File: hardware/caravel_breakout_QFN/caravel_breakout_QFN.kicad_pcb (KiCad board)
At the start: 2 copper layers, 25.4 x 25.4 mm, 20 parts, among them J1 Conn_01x14_Female, J2 Conn_01x14_Female, J3 Conn_01x14_Female, J4 Conn_01x14_Female, T1 Logo, T2 Logo, U1 Caravel

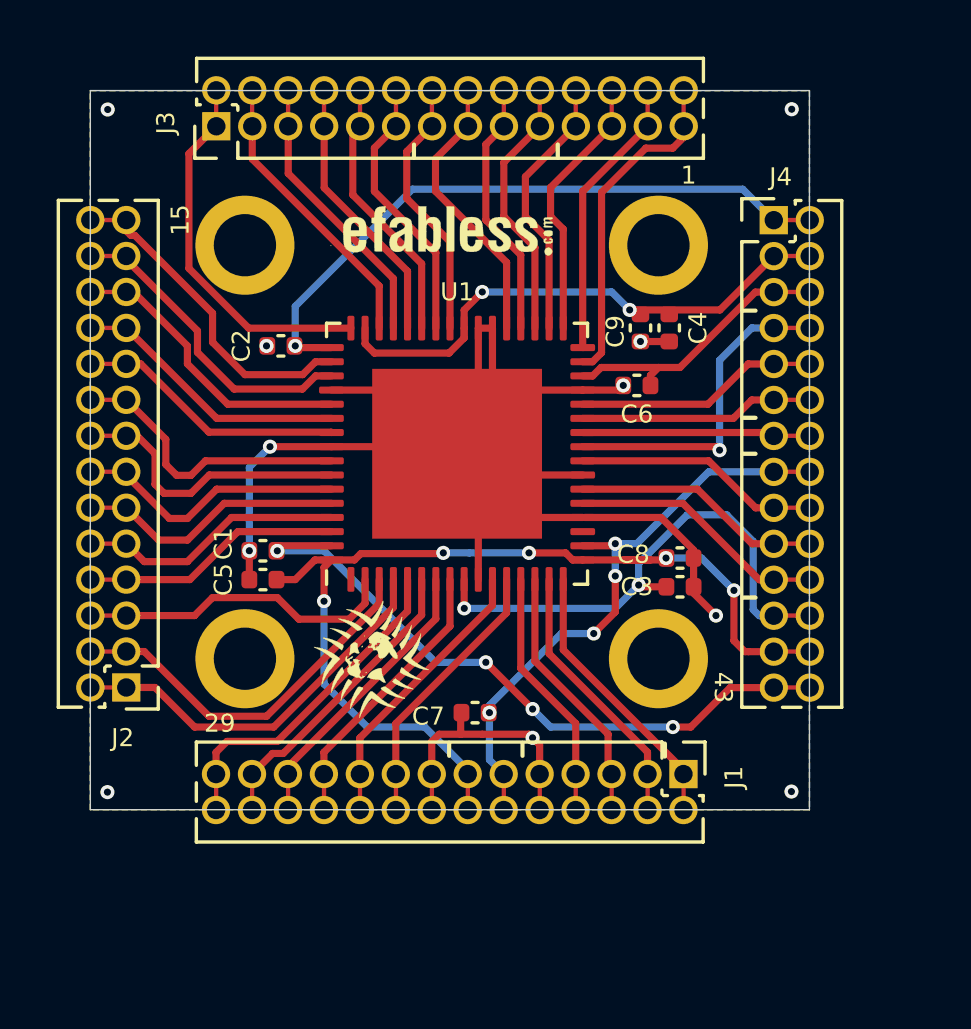
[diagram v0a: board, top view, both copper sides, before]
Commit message: Updated the caravel QFN breakout board connectors
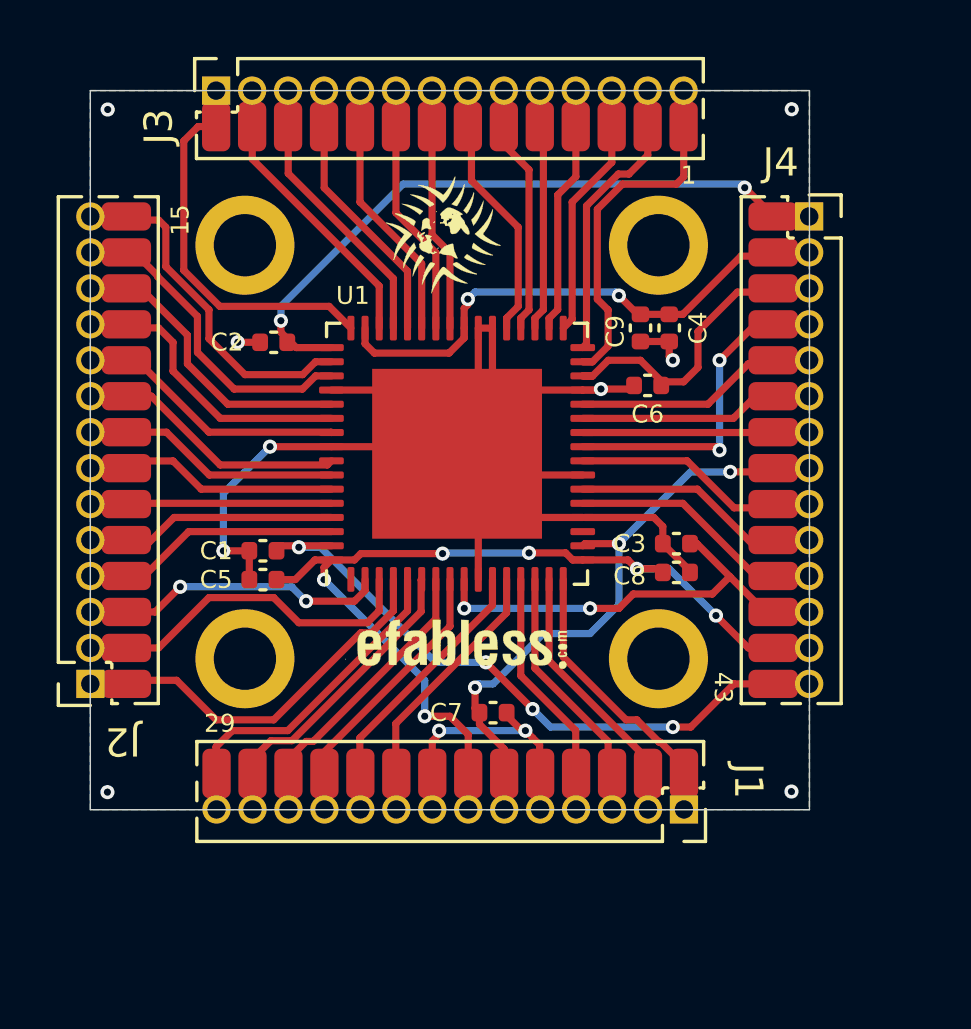
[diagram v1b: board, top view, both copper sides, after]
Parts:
- J1, J2, J3, J4: footprint Connector_PinHeader_1.27mm:PinHeader_2x14_P1.27mm_Vertical -> Caravel_Board:Caravel_Breakout_Connectors_2x14
- T2: footprint Caravel:ef_logo -> Caravel_Board:ef_logo
- moved T1 15.2 mm to (132.8, 81.3)
- moved T2 14.6 mm to (133.5, 95.8)
- moved C3 1.53 mm to (141.1, 92.2), turned to 0 degrees
- moved J4 1.42 mm to (145.2, 79.5)
- moved J1 1.31 mm to (142.5, 101.0)
- moved J3 1.31 mm to (123.7, 76.8)
- moved J2 1.20 mm to (121.0, 98.3)
- moved C7 0.63 mm to (134.6, 98.2), turned to 180 degrees
- moved C8 0.52 mm to (141.1, 93.2)
- moved C6 0.38 mm to (140.1, 86.6)
- moved C2 0.28 mm to (126.9, 85.1)
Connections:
- J1 pad 10: GND -> mprj_io[32]
- J1 pad 11: vccd -> mprj_io[31]
- J1 pad 12: vccd -> mprj_io[30]
- J1 pad 13: vddio -> mprj_io[29]
- J1 pad 14: vddio -> mprj_io[28]
- J1 pad 2: mprj_io[37] -> mprj_io[36]
- J1 pad 3: mprj_io[36] -> mprj_io[35]
- J1 pad 4: mprj_io[36] -> mprj_io[34]
- J1 pad 5: mprj_io[35] -> GND
- J1 pad 6: mprj_io[35] -> vccd
- J1 pad 7: mprj_io[34] -> vddio
- J1 pad 8: mprj_io[34] -> GND
- J1 pad 9: GND -> mprj_io[33]
- J2 pad 10: mprj_io[23] -> mprj_io[18]
- J2 pad 11: mprj_io[22] -> mprj_io[17]
- J2 pad 12: mprj_io[22] -> mprj_io[16]
- J2 pad 13: mprj_io[21] -> mprj_io[15]
- J2 pad 14: mprj_io[21] -> mprj_io[14]
- J2 pad 2: mprj_io[27] -> mprj_io[26]
- J2 pad 3: mprj_io[26] -> mprj_io[25]
- J2 pad 4: mprj_io[26] -> mprj_io[24]
- J2 pad 5: mprj_io[25] -> mprj_io[23]
- J2 pad 6: mprj_io[25] -> mprj_io[22]
- J2 pad 7: mprj_io[24] -> mprj_io[21]
- J2 pad 8: mprj_io[24] -> mprj_io[20]
- J2 pad 9: mprj_io[23] -> mprj_io[19]
- J3 pad 10: mprj_io[9] -> mprj_io[4]_SCK
- J3 pad 11: mprj_io[8] -> mprj_io[3]_CSB
- J3 pad 12: mprj_io[8] -> mprj_io[2]_SDI
- J3 pad 13: mprj_io[7] -> mprj_io[1]_SDO
- J3 pad 14: mprj_io[7] -> mprj_io[0]
- J3 pad 2: mprj_io[13] -> mprj_io[12]
- J3 pad 3: mprj_io[12] -> mprj_io[11]
- J3 pad 4: mprj_io[12] -> mprj_io[10]
- J3 pad 5: mprj_io[11] -> mprj_io[9]
- J3 pad 6: mprj_io[11] -> mprj_io[8]
- J3 pad 7: mprj_io[10] -> mprj_io[7]
- J3 pad 8: mprj_io[10] -> mprj_io[6]_ser_tx
- J3 pad 9: mprj_io[9] -> mprj_io[5]_ser_rx
- J4 pad 10: gpio -> xclk
- J4 pad 11: Caravel_D1 -> ~{RST}
- J4 pad 12: Caravel_D1 -> vdda2
- J4 pad 13: Caravel_D0 -> vddio
- J4 pad 14: Caravel_D0 -> vccd2
- J4 pad 2: vccd1 -> vdda1
- J4 pad 3: vdda1 -> vdda
- J4 pad 4: vdda1 -> Caravel_SCK
- J4 pad 5: vdda -> gpio
- J4 pad 6: vdda -> Caravel_D1
- J4 pad 7: Caravel_SCK -> Caravel_D0
- J4 pad 8: Caravel_SCK -> vccd
- J4 pad 9: gpio -> Caravel_CSB
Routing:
- net GND: track 68.7 -> 63.4 mm
- net vddio: track 34.7 -> 30.4 mm, vias 5 -> 6
- net vdda2: track 18.7 -> 15.3 mm
- net mprj_io[20]: track 10.1 -> 7.93 mm
- net mprj_io[26]: track 13.5 -> 11.3 mm
- net mprj_io[22]: track 9.32 -> 7.31 mm
- net mprj_io[8]: track 9.55 -> 7.71 mm
- net mprj_io[19]: track 10.2 -> 8.32 mm
- net vccd2: track 23.7 -> 21.9 mm
- net mprj_io[7]: track 9.20 -> 7.39 mm
- net mprj_io[3]_CSB: track 9.28 -> 7.52 mm
- net mprj_io[21]: track 9.50 -> 7.82 mm
- net mprj_io[6]_ser_tx: track 9.71 -> 8.03 mm
- net mprj_io[23]: track 9.22 -> 7.63 mm
- net mprj_io[25]: track 11.2 -> 9.56 mm, vias 0 -> 2
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
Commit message: add gerber files
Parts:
- U1: footprint Package_DFN_QFN:QFN-64-1EP_9x9mm_P0.5mm_EP6x6mm -> Package_DFN_QFN:QFN-64-1EP_9x9mm_P0.5mm_EP7.65x7.65mm
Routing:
- net vdda1: track 17.7 -> 19.4 mm, vias 2 -> 3
- net vddio: track 30.4 -> 31.6 mm, vias 6 -> 4
- net vccd2: track 21.9 -> 22.9 mm

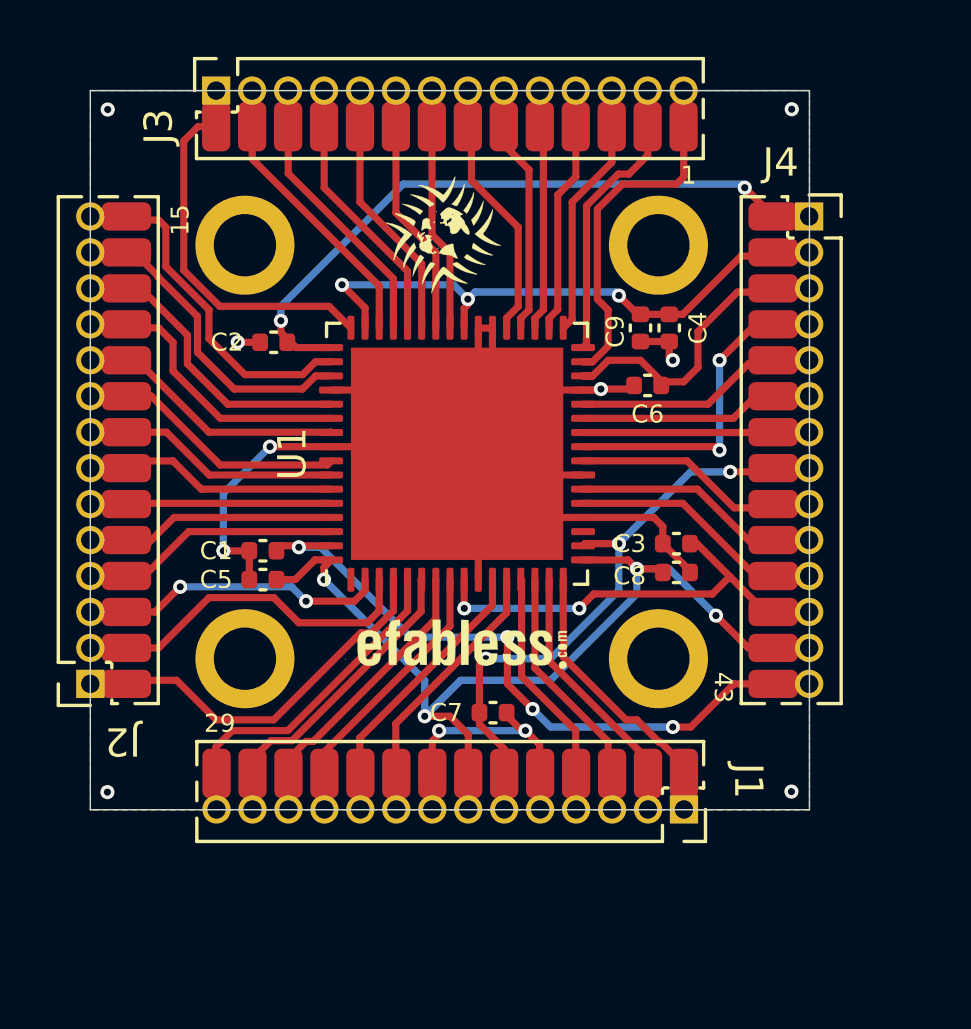
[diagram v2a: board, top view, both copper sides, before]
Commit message: add pads on both sides of caravel breakout board (Rev C)
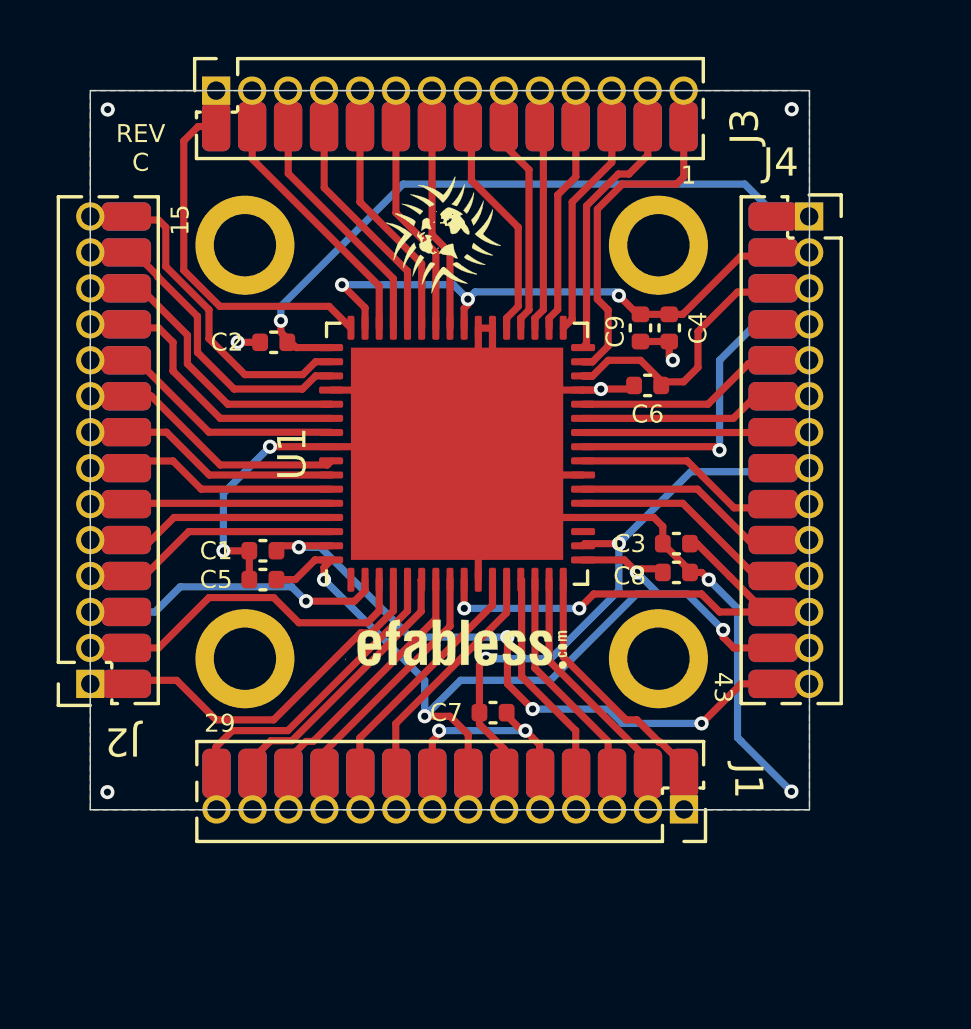
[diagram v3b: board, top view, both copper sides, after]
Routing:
- net GND: track 63.4 -> 72.9 mm, vias 11 -> 12
- net vdda2: track 15.3 -> 16.1 mm
- net vccd1: track 22.5 -> 22.7 mm, vias 2 -> 1
- net vccd: vias 3 -> 2
- net mprj_io[25]: vias 2 -> 1
- net Caravel_SCK: vias 2 -> 1
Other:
- board text added: "C"
- board text added: "REV"

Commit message: update QFN caravel breakout board silkscreen
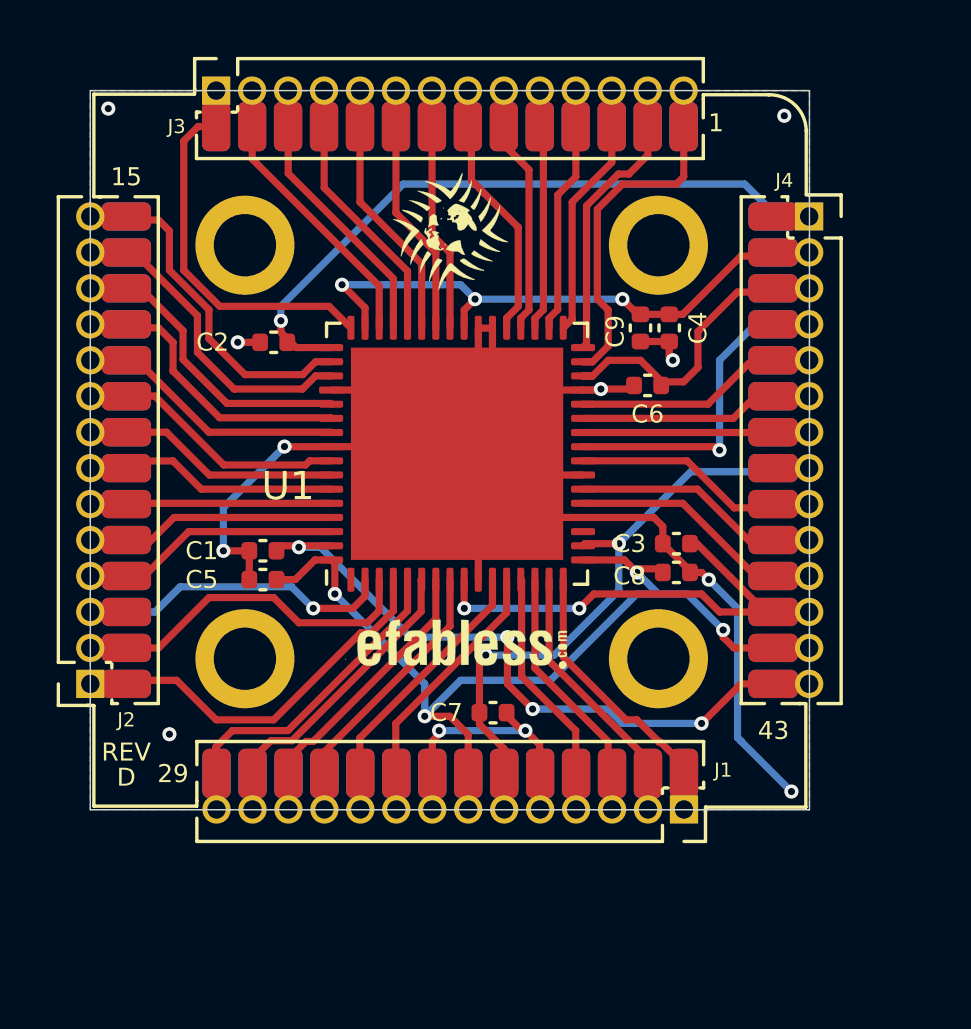
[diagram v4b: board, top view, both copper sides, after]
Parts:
- added ?: , clipboard:dd7ec026-37c5-4c16-b24b-a4168c525ae3, F.Cu at (145.3, 76.7)
- moved T1 0.28 mm to (133.1, 81.2)
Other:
- board text added: "D"
- board text removed: "C"

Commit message: update caravel QFN breakout board with WCSP pinout (V2)
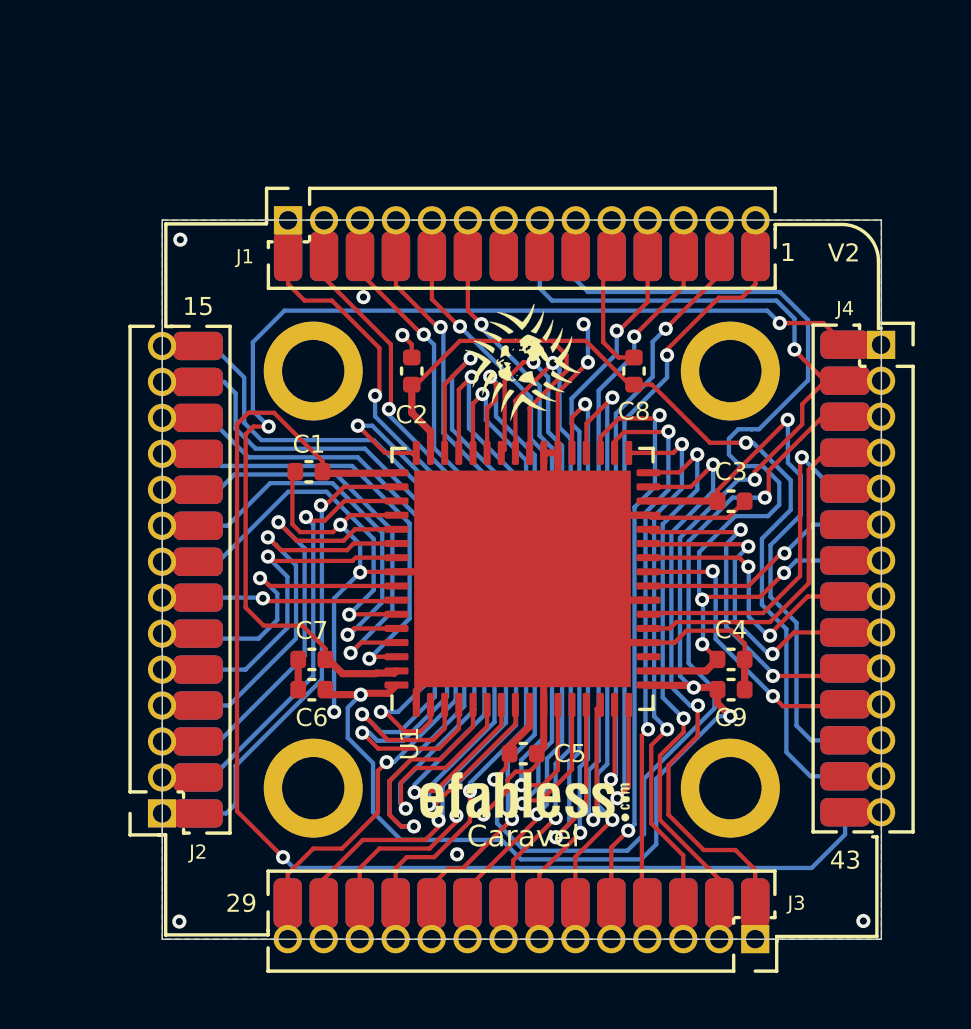
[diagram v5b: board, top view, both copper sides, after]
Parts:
- removed ?: , clipboard:dd7ec026-37c5-4c16-b24b-a4168c525ae3
- T2: footprint Caravel_Board:ef_logo -> Caravel:ef_logo
- moved J3 35.8 mm to (145.0, 105.5), turned to -90 degrees
- moved J1 25.4 mm to (126.2, 81.4), turned to 90 degrees
- moved C6 16.0 mm to (128.2, 97.4), turned to 0 degrees
- moved C9 13.2 mm to (143.0, 97.4), turned to 180 degrees
- moved C4 11.9 mm to (143.0, 96.3), turned to 180 degrees
- moved C5 11.1 mm to (135.7, 99.6), turned to 180 degrees
- moved C8 7.27 mm to (139.6, 86.1), turned to 90 degrees
- moved C7 6.67 mm to (128.2, 96.3), turned to 0 degrees
- moved T2 5.82 mm to (135.7, 101.1)
- moved T1 5.27 mm to (135.6, 85.8)
- moved H2 5.23 mm to (143.0, 100.8)
- moved J2 5.23 mm to (123.6, 102.9)
- moved J4 5.20 mm to (147.7, 84.0)
- moved H1 5.17 mm to (128.3, 100.8)
- moved H3 5.12 mm to (143.0, 86.1)
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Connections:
- C1 pad 2: vccd2 -> vccd1
- C2 pad 1: GND -> vdda1
- C2 pad 2: vccd1 -> GND
- C3 pad 1: GND -> vdda
- C3 pad 2: vdda2 -> GND
- C4 pad 1: vdda1 -> GND
- C4 pad 2: GND -> vccd
- C5 pad 2: vddio -> vdda2
- C6 pad 1: vdda -> GND
- C6 pad 2: GND -> vddio
- C7 pad 2: vccd -> vccd2
- C8 pad 1: GND -> vdda1
- C8 pad 2: vddio -> GND
- C9 pad 1: vdda1 -> GND
- C9 pad 2: GND -> vddio
- J1 pad 1: mprj_io[37] -> mprj_io[28]
- J1 pad 10: mprj_io[32] -> GND
- J1 pad 11: mprj_io[31] -> mprj_io[34]
- J1 pad 12: mprj_io[30] -> mprj_io[35]
- J1 pad 13: mprj_io[29] -> mprj_io[36]
- J1 pad 14: mprj_io[28] -> mprj_io[37]
- J1 pad 2: mprj_io[36] -> mprj_io[29]
- J1 pad 3: mprj_io[35] -> mprj_io[30]
- J1 pad 4: mprj_io[34] -> mprj_io[31]
- J1 pad 5: GND -> mprj_io[32]
- J1 pad 6: vccd -> mprj_io[33]
- J1 pad 7: vddio -> GND
- J1 pad 8: GND -> vddio
- J1 pad 9: mprj_io[33] -> vccd
- J2 pad 1: mprj_io[27] -> mprj_io[14]
- J2 pad 10: mprj_io[18] -> mprj_io[23]
- J2 pad 11: mprj_io[17] -> mprj_io[24]
- J2 pad 12: mprj_io[16] -> mprj_io[25]
- J2 pad 13: mprj_io[15] -> mprj_io[26]
- J2 pad 14: mprj_io[14] -> mprj_io[27]
- J2 pad 2: mprj_io[26] -> mprj_io[15]
- J2 pad 3: mprj_io[25] -> mprj_io[16]
- J2 pad 4: mprj_io[24] -> mprj_io[17]
- J2 pad 5: mprj_io[23] -> mprj_io[18]
- J2 pad 6: mprj_io[22] -> mprj_io[19]
- J2 pad 7: mprj_io[21] -> mprj_io[20]
- J2 pad 8: mprj_io[20] -> mprj_io[21]
- J2 pad 9: mprj_io[19] -> mprj_io[22]
- J3 pad 1: mprj_io[13] -> mprj_io[0]
- J3 pad 10: mprj_io[4]_SCK -> mprj_io[9]
- J3 pad 11: mprj_io[3]_CSB -> mprj_io[10]
- J3 pad 12: mprj_io[2]_SDI -> mprj_io[11]
- J3 pad 13: mprj_io[1]_SDO -> mprj_io[12]
- J3 pad 14: mprj_io[0] -> mprj_io[13]
- J3 pad 2: mprj_io[12] -> mprj_io[1]_SDO
- J3 pad 3: mprj_io[11] -> mprj_io[2]_SDI
- J3 pad 4: mprj_io[10] -> mprj_io[3]_CSB
- J3 pad 5: mprj_io[9] -> mprj_io[4]_SCK
- J3 pad 6: mprj_io[8] -> mprj_io[5]_ser_rx
- J3 pad 7: mprj_io[7] -> mprj_io[6]_ser_tx
- J3 pad 8: mprj_io[6]_ser_tx -> mprj_io[7]
- J3 pad 9: mprj_io[5]_ser_rx -> mprj_io[8]
- J4 pad 1: vccd1 -> vccd2
- J4 pad 10: xclk -> gpio
- J4 pad 11: ~{RST} -> Caravel_SCK
- J4 pad 12: vdda2 -> vdda
- J4 pad 13: vddio -> vdda1
- J4 pad 14: vccd2 -> vccd1
- J4 pad 2: vdda1 -> vddio
- J4 pad 3: vdda -> vdda2
- J4 pad 4: Caravel_SCK -> ~{RST}
- J4 pad 5: gpio -> xclk
- J4 pad 6: Caravel_D1 -> Caravel_CSB
- J4 pad 7: Caravel_D0 -> vccd
- J4 pad 8: vccd -> Caravel_D0
- J4 pad 9: Caravel_CSB -> Caravel_D1
- U1 pad 1: unconnected-(U1-Pad1) -> GND
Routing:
- net vddio: track 31.5 -> 56.4 mm, vias 4 -> 5
- net vccd1: track 22.7 -> 47.2 mm
- net mprj_io[28]: track 10.8 -> 31.9 mm, vias 0 -> 2
- net mprj_io[34]: track 7.67 -> 28.3 mm, vias 0 -> 2
- net mprj_io[12]: track 8.99 -> 29.1 mm, vias 0 -> 2
- net mprj_io[29]: track 9.77 -> 28.6 mm, vias 0 -> 2
- net mprj_io[35]: track 8.00 -> 26.6 mm, vias 0 -> 2
- net vdda1: track 19.3 -> 37.3 mm, vias 3 -> 1
- net mprj_io[31]: track 8.72 -> 26.7 mm, vias 0 -> 2
- net mprj_io[11]: track 8.67 -> 26.5 mm, vias 0 -> 2
- net mprj_io[30]: track 9.19 -> 26.6 mm, vias 0 -> 2
- net mprj_io[7]: track 7.39 -> 24.6 mm, vias 0 -> 2
- net mprj_io[9]: track 8.03 -> 25.2 mm, vias 0 -> 2
- net vccd: track 19.8 -> 36.9 mm, vias 2 -> 3
- net mprj_io[8]: track 7.71 -> 24.8 mm, vias 0 -> 2
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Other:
- board text added: "Caravel"
- board text added: "V2"
- board text removed: "D"
- board text removed: "REV"
